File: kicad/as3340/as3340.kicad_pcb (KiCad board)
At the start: 4 copper layers, 80 x 80 mm, 141 parts, among them J3 Conn_02x20_Odd_Even, U1 TL074, U10 LM79L05, U11 LM393, U12 TL074, U13 LM4040AIM3-2.5, U14 TLV5610IDW, U15 M24C02-WMN, U2 TL074, U3 AS3340, U4 PS508, U5 MAX333A, U6 AS3360, U7 PCA9555D, U8 DG442CY+, U9 DG442CY+

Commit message: kicad6 commit
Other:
- net class Default removed

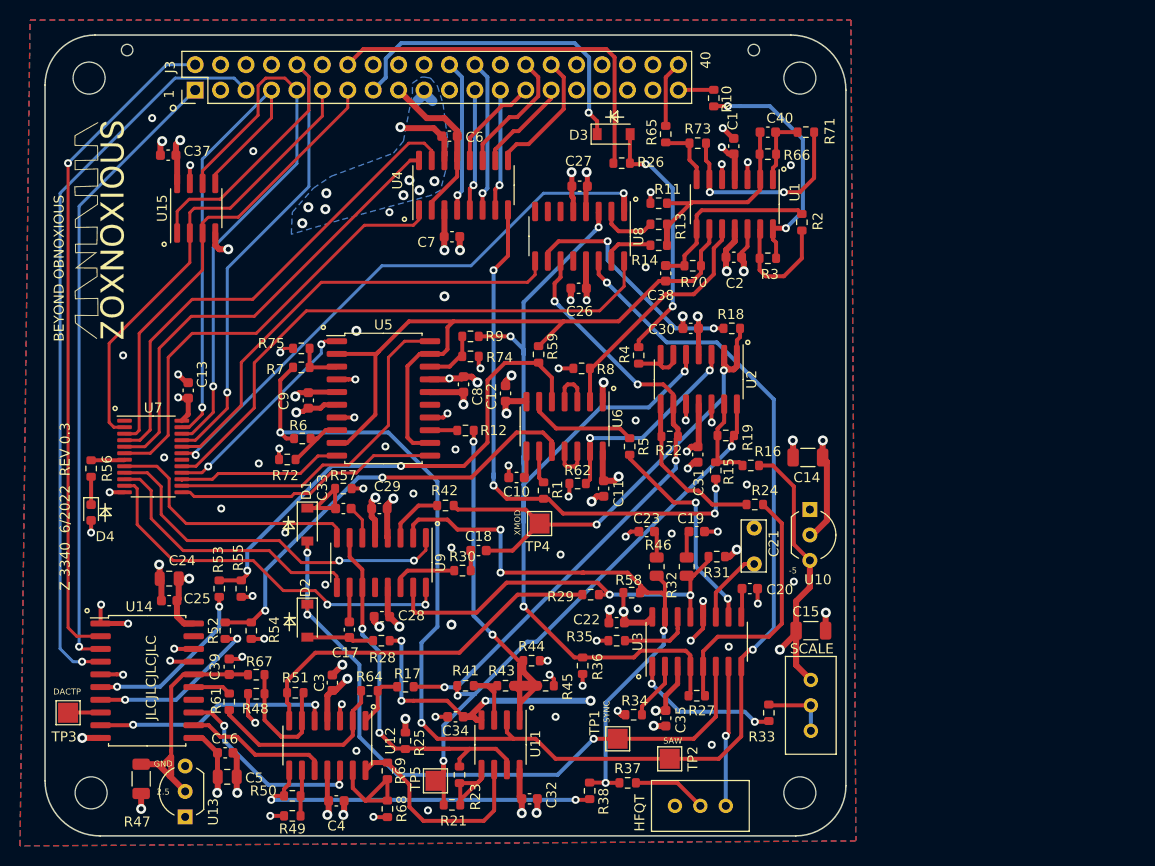
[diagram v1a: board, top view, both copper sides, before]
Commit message: schematic changes, still need values
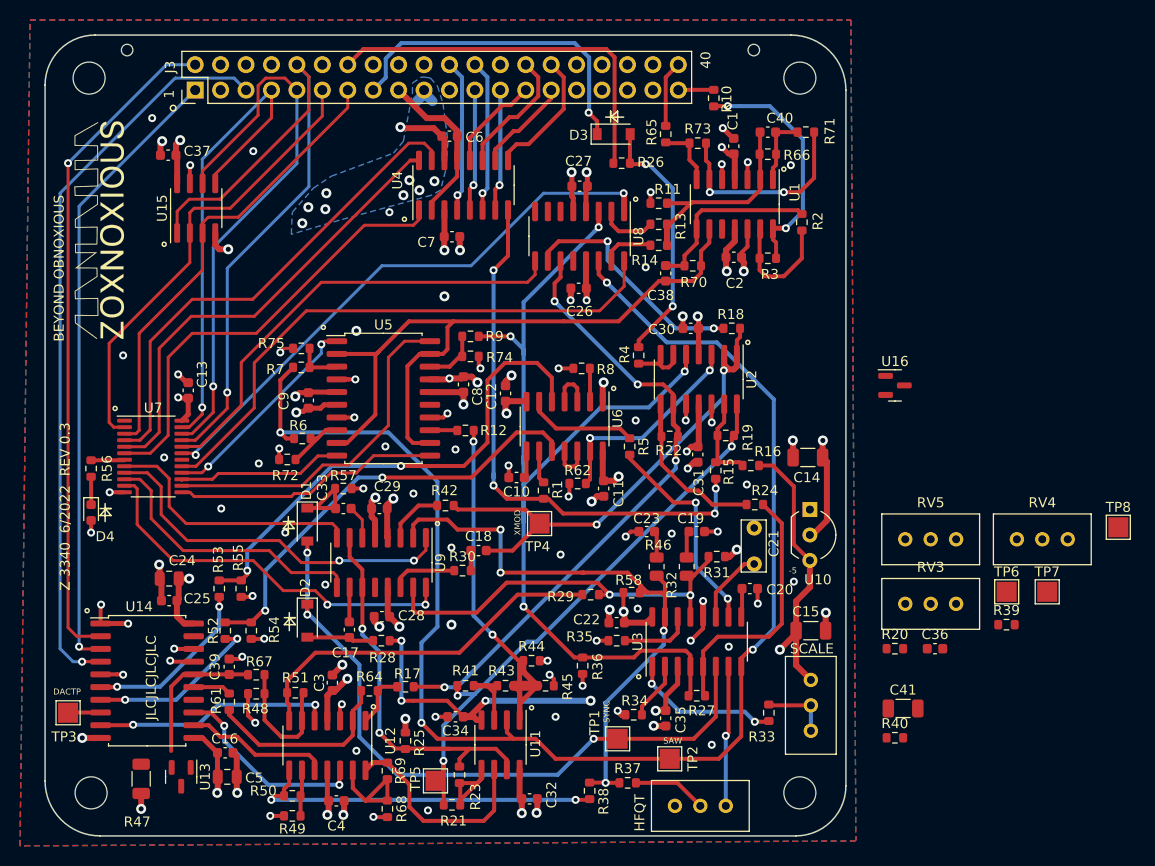
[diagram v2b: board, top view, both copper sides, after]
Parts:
- removed R59: 24k, Resistor_SMD:R_0603_1608Metric
- added C36: 470p, Capacitor_SMD:C_0603_1608Metric, F.Cu at (155.9, 86.8)
- added C41: 2.2u, Capacitor_SMD:C_1206_3216Metric, F.Cu at (152.7, 92.8)
- added R20: 5k6, Resistor_SMD:R_0603_1608Metric, F.Cu at (151.9, 86.8)
- added R39: 22k, Resistor_SMD:R_0603_1608Metric, F.Cu at (163.0, 84.4)
- added R40: ?, Resistor_SMD:R_0603_1608Metric, F.Cu at (151.9, 95.7)
- added RV3: 10K, Potentiometer_THT:Potentiometer_Bourns_3296W_Vertical, F.Cu at (158.0, 82.3)
- added RV4: 500, Potentiometer_THT:Potentiometer_Bourns_3296W_Vertical, F.Cu at (169.2, 75.9)
- added RV5: 100k, Potentiometer_THT:Potentiometer_Bourns_3296W_Vertical, F.Cu at (158.0, 75.9)
- added TP6: TestPoint, TestPoint:TestPoint_Pad_2.0x2.0mm, F.Cu at (163.1, 81.1)
- added TP7: TestPoint, TestPoint:TestPoint_Pad_2.0x2.0mm, F.Cu at (167.1, 81.1)
- added TP8: TestPoint, TestPoint:TestPoint_Pad_2.0x2.0mm, F.Cu at (174.2, 74.7)
- added U16: LM4040CIM3-2.5, Package_TO_SOT_SMD:SOT-23, F.Cu at (151.9, 60.5)
- R31: value 1.5M -> 1M5
- R33: value 20K -> 13k
- R35: value 1K82 -> 1k6
- R42: value 300k -> 200k
- R58: value 220k -> 200k
- R69: value 30k -> 10k
- R72: value 180k -> ?
- R74: value 220k -> ?
- R75: value 360k -> ?
- U13: footprint Package_TO_SOT_THT:TO-92_Inline_Wide -> Package_TO_SOT_SMD:SOT-23
- moved U13 4.02 mm to (80.6, 99.6), turned to -90 degrees
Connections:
- J3 pad 21: GND -> /CARD1_OUT1
- J3 pad 22: /CARD1_OUT1 -> /CARD1_OUT2
- J3 pad 23: /CARD1_OUT2 -> /CARD2_OUT1
- J3 pad 24: /CARD2_OUT1 -> GND
- J3 pad 26: GND -> /CARD3_OUT1
- J3 pad 27: /CARD3_OUT1 -> /CARD3_OUT2
- J3 pad 28: /CARD3_OUT2 -> GND
- J3 pad 36: /CARD7_OUT1 -> GND
- J3 pad 37: /CARD7_OUT2 -> /CARD7_OUT1
- R31 pad 1: +12V -> Net-(R31-Pad1)
- R35 pad 2: GND -> Net-(R35-Pad2)
- R58 pad 1: +12V -> Net-(R58-Pad1)
- R72 pad 1: -12V -> /Output Mix/OFFSET_REF-2.5
- R74 pad 1: -12V -> /Output Mix/OFFSET_REF-2.5
- R75 pad 1: -12V -> /Output Mix/OFFSET_REF-2.5
- R8 pad 2: /Output Mix/MIX1_NONINV -> /Output Mix/VCA_TRI
- RV1 pad 1: Net-(R33-Pad2) -> Net-(RV1-Pad1)
- RV1 pad 2: Net-(R33-Pad2) -> Net-(RV1-Pad1)
- RV1 pad 3: -5V -> Net-(R33-Pad2)
- U1 pad 10: /Output Mix/MIX1_NONINV -> GND
- U14 pad 14: Net-(U14-Pad14) -> unconnected-(U14-Pad14)
- U14 pad 19: Net-(U14-Pad19) -> unconnected-(U14-Pad19)
- U4 pad 10: /CARD4_OUT1 -> /CARD6_OUT1
- U4 pad 11: /CARD3_OUT2 -> /CARD5_OUT1
- U4 pad 12: /CARD3_OUT1 -> /CARD4_OUT1
- U4 pad 7: /CARD2_OUT2 -> /CARD3_OUT1
- U4 pad 9: /CARD4_OUT2 -> /CARD7_OUT1
- U5 pad 15: Net-(U5-Pad15) -> unconnected-(U5-Pad15)
- U6 pad 2: /Output Mix/MIX1_NONINV -> /Output Mix/VCA_TRI
- U7 pad 1: Net-(U7-Pad1) -> unconnected-(U7-Pad1)
- U7 pad 18: Net-(U7-Pad18) -> unconnected-(U7-Pad18)
- U8 pad 12: Net-(U8-Pad12) -> unconnected-(U8-Pad12)
- U8 pad 6: Net-(U8-Pad6) -> unconnected-(U8-Pad6)
- U8 pad 7: Net-(U8-Pad7) -> unconnected-(U8-Pad7)
- U8 pad 8: Net-(U8-Pad8) -> unconnected-(U8-Pad8)
- U9 pad 12: Net-(U9-Pad12) -> unconnected-(U9-Pad12)
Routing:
- net /Output Mix/MIX1_NONINV: track 24.5 -> 0.00 mm
- net /CARD7_OUT1: track 0.00 -> 13.1 mm
- net /CARD4_OUT2: track 13.1 -> 0.00 mm
- net /CARD5_OUT1: track 0.00 -> 12.8 mm
- net /CARD3_OUT2: track 12.8 -> 0.00 mm
- net /CARD2_OUT2: track 12.2 -> 0.00 mm, vias 1 -> 0
- net /DAC/VREF_2.5V: track 26.0 -> 14.6 mm
- net /CARD6_OUT1: track 0.00 -> 9.63 mm
- net Net-(RV1-Pad1): track 0.00 -> 6.98 mm
- net Net-(R33-Pad2): track 6.98 -> 0.00 mm
- net -12V: track 51.9 -> 48.1 mm, vias 20 -> 17
- net /Output Mix/OFFSET_REF-2.5: track 0.00 -> 3.82 mm, vias 0 -> 3
- net /Output Mix/MIX1_INV: track 76.8 -> 73.3 mm
- net /Output Mix/VCA_TRI: track 0.00 -> 3.33 mm
- net /CARD3_OUT1: track 9.82 -> 12.2 mm, vias 0 -> 1
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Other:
- board text removed: "2.5"
- board text removed: "GND"

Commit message: going back to two trimmer method
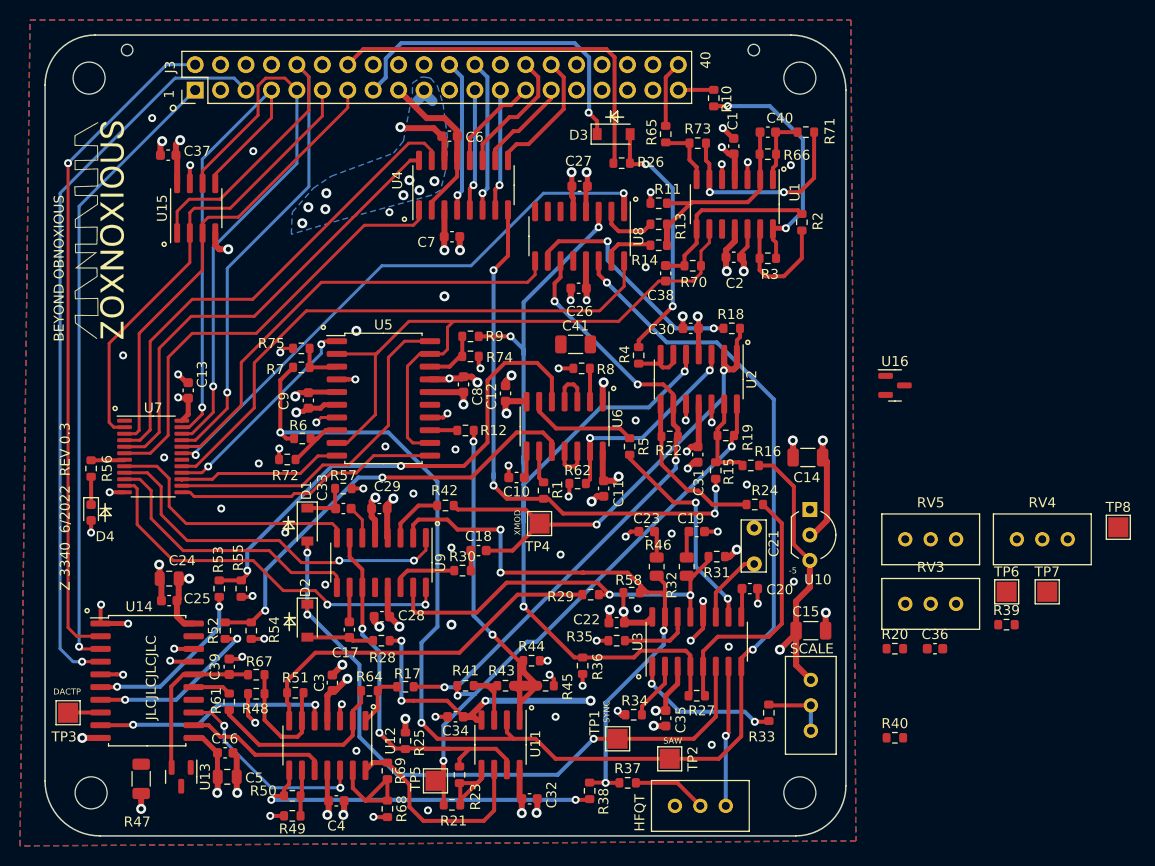
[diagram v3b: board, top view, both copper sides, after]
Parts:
- moved C41 48.9 mm to (120.0, 56.4)
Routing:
- net Net-(C33-Pad1): track 8.38 -> 5.62 mm
- net /DAC/VREF_2.5V: track 14.6 -> 16.3 mm
- net /DAC/SYNC_LEVEL_FROM_DAC: track 19.9 -> 20.4 mm
- net GND: track 271.2 -> 271.7 mm

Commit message: pcb cleanup, get volt ref in
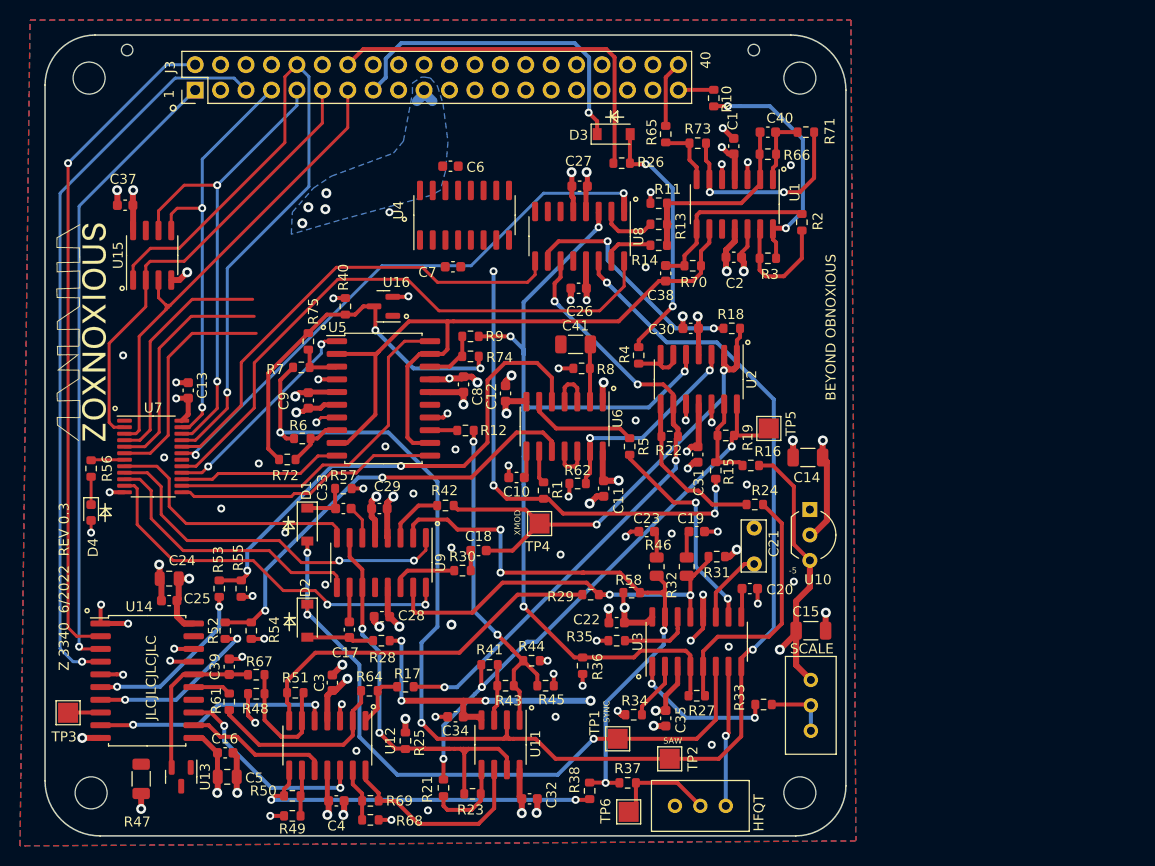
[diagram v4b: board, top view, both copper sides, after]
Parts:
- removed C36: 470p, Capacitor_SMD:C_0603_1608Metric
- removed R20: 5k6, Resistor_SMD:R_0603_1608Metric
- removed R39: 22k, Resistor_SMD:R_0603_1608Metric
- removed RV3: 10K, Potentiometer_THT:Potentiometer_Bourns_3296W_Vertical
- removed RV4: 500, Potentiometer_THT:Potentiometer_Bourns_3296W_Vertical
- removed RV5: 100k, Potentiometer_THT:Potentiometer_Bourns_3296W_Vertical
- removed TP7, TP8: TestPoint, TestPoint:TestPoint_Pad_2.0x2.0mm
- R33: value 13k -> 24k
- R35: value 1k6 -> 1k8
- R58: value 200k -> 300k
- moved R40 69.8 mm to (97.0, 52.6), turned to -90 degrees
- moved U16 51.7 mm to (100.8, 52.6), turned to 180 degrees
- moved TP5 48.5 mm to (139.3, 64.8)
- moved TP6 43.7 mm to (125.3, 103.1)
- moved G*** 10.4 mm to (70.6, 55.2)
- moved C37 6.59 mm to (75.0, 42.5)
- moved U15 6.44 mm to (77.7, 47.5)
- moved R69 3.45 mm to (99.5, 102.0), turned to 180 degrees
- moved R41 3.19 mm to (111.4, 88.4)
- moved U4 3.00 mm to (108.9, 43.5)
- moved C6 3.00 mm to (107.5, 38.6)
- moved C7 3.00 mm to (107.8, 48.6)
- moved R23 2.30 mm to (109.7, 101.3), turned to 0 degrees
- moved R68 2.02 mm to (99.5, 103.9), turned to 0 degrees
- moved R21 1.90 mm to (106.8, 100.7), turned to 90 degrees
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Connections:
- R31 pad 1: Net-(R31-Pad1) -> +12V
- R35 pad 2: Net-(R35-Pad2) -> GND
- R58 pad 1: Net-(R58-Pad1) -> +12V
- RV1 pad 1: Net-(RV1-Pad1) -> Net-(R33-Pad2)
- RV1 pad 2: Net-(RV1-Pad1) -> Net-(R33-Pad2)
- RV1 pad 3: Net-(R33-Pad2) -> -5V
- TP6 pad 1: Net-(RV1-Pad1) -> Net-(R37-Pad2)
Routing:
- net /Output Mix/OFFSET_REF-2.5: track 3.82 -> 38.2 mm, vias 3 -> 2
- net /EXT_MOD_SEL_CTRL2: track 49.4 -> 23.8 mm
- net /EXT_MOD_SEL_CTRL1: track 46.2 -> 23.3 mm
- net /EXT_MOD_SEL_CTRL0: track 44.6 -> 22.7 mm
- net +12V: track 67.0 -> 46.6 mm, vias 12 -> 13
- net /VCO_COMP: track 52.7 -> 34.7 mm
- net /CARD2_OUT1: track 15.2 -> 0.00 mm, vias 1 -> 0
- net /CARD1_OUT1: track 15.2 -> 0.00 mm, vias 1 -> 0
- net /CARD7_OUT1: track 13.1 -> 0.00 mm
- net /CARD5_OUT1: track 12.8 -> 0.00 mm
- net /CARD3_OUT1: track 12.2 -> 0.00 mm, vias 1 -> 0
- net /CARD1_OUT2: track 12.2 -> 0.00 mm, vias 1 -> 0
- net /CARD4_OUT1: track 9.82 -> 0.00 mm
- net /CARD6_OUT1: track 9.63 -> 0.00 mm
- net /SCL1: track 56.4 -> 48.6 mm, vias 1 -> 2
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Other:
- board text removed: "DACTP"

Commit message: moved 2x20 5mm back
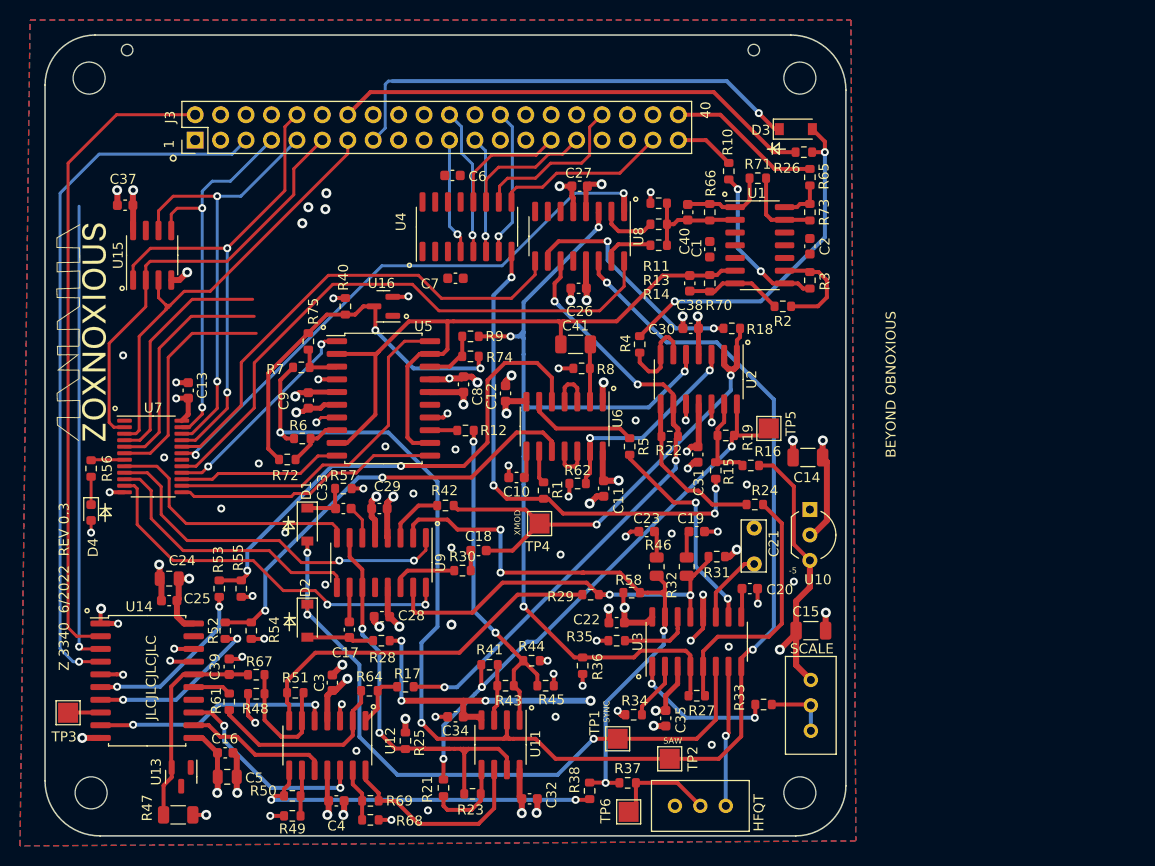
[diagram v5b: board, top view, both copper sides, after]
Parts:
- moved R26 18.2 mm to (142.8, 37.2)
- moved D3 18.2 mm to (142.0, 34.9)
- moved R65 15.0 mm to (143.4, 39.7)
- moved R73 13.2 mm to (143.4, 43.2), turned to -90 degrees
- moved C40 11.3 mm to (131.2, 43.2), turned to -90 degrees
- moved C1 10.6 mm to (133.4, 46.9), turned to -90 degrees
- moved R2 8.61 mm to (140.7, 52.6), turned to 180 degrees
- moved R66 8.20 mm to (133.4, 43.2), turned to 90 degrees
- moved C2 7.68 mm to (143.4, 46.6), turned to -90 degrees
- moved R10 7.45 mm to (135.3, 39.1)
- moved R71 6.65 mm to (138.2, 39.8)
- moved R47 5.16 mm to (80.3, 103.4), turned to 180 degrees
- moved J3 5.00 mm to (82.0, 36.0)
- moved U1 4.80 mm to (138.4, 46.5), turned to 0 degrees
- moved R3 4.74 mm to (143.4, 50.0), turned to 90 degrees
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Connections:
- U1 pad 13: Net-(R2-Pad1) -> Net-(R71-Pad1)
- U1 pad 14: Net-(R10-Pad1) -> Net-(R65-Pad1)
- U1 pad 6: Net-(R71-Pad1) -> /Output Mix/MIX1_INV
- U1 pad 7: Net-(R65-Pad1) -> Net-(C38-Pad1)
- U1 pad 8: Net-(C38-Pad1) -> Net-(R10-Pad1)
- U1 pad 9: /Output Mix/MIX1_INV -> Net-(R2-Pad1)
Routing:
- net /I2C_ADDR0: track 74.0 -> 49.6 mm, vias 1 -> 2
- net /CARD7_OUT1: track 0.00 -> 17.3 mm
- net /CARD6_OUT1: track 0.00 -> 16.4 mm
- net /SPI_CLK: track 62.6 -> 46.2 mm
- net /CARD3_OUT1: track 0.00 -> 14.7 mm, vias 0 -> 1
- net /CARD1_OUT2: track 0.00 -> 14.7 mm, vias 0 -> 1
- net /CARD5_OUT1: track 0.00 -> 12.9 mm
- net Net-(R71-Pad1): track 20.6 -> 8.25 mm, vias 2 -> 0
- net /CARD4_OUT1: track 0.00 -> 12.0 mm
- net /CARD2_OUT1: track 0.00 -> 11.6 mm, vias 0 -> 1
- net /CARD1_OUT1: track 0.00 -> 11.6 mm, vias 0 -> 1
- net GND: track 264.0 -> 253.1 mm, vias 83 -> 76
- net /GPIO_MODULE_DRIVEN: track 38.3 -> 48.2 mm
- net +5V: track 66.7 -> 76.4 mm
- net Net-(D3-Pad2): track 25.5 -> 35.2 mm
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- removed copper zone on B.Cu, net -12V

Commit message: initial routing done
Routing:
- net -12V: track 38.0 -> 101.7 mm, vias 12 -> 16
- net GND: track 253.1 -> 279.4 mm, vias 76 -> 83
- net /EXT_MOD_SEL_CTRL2: track 23.8 -> 48.0 mm
- net /EXT_MOD_SEL_CTRL1: track 23.3 -> 45.6 mm
- net /EXT_MOD_SEL_CTRL0: track 22.7 -> 44.7 mm
- net +12V: track 42.6 -> 62.6 mm, vias 12 -> 13
- net /SPI_CLK: track 46.2 -> 62.3 mm, vias 1 -> 0
- net -5V: track 92.9 -> 87.9 mm
- net /SPI_MOSI: track 64.7 -> 61.4 mm, vias 0 -> 1
- net /SPI_CS0: track 70.9 -> 72.1 mm, vias 1 -> 0
- net Net-(R61-Pad1): track 20.2 -> 19.3 mm
- net Net-(C33-Pad1): track 5.62 -> 4.80 mm
- net /cem3340/SUMMING_INPUT: track 60.0 -> 59.2 mm
- net Net-(D3-Pad2): track 35.2 -> 34.5 mm
- added copper zone on B.Cu, net -12V
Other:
- board text added: "Z3340 9/2022 REV 0.4"
- board text removed: "Z 3340 6/2022 REV 0.3"
